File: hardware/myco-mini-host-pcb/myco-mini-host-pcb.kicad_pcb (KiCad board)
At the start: 2 copper layers, 190 x 115 mm, 22 parts, among them J1 Conn_01x17_Female, J2 Conn_01x17_Female, Q1 AO3401A, Q2 AO3401A, SW1 EM-04-Q, U1 XC9145B33C0R-G, U2 SHT40-AD1B-R2, U3 BH1750FVI-TR

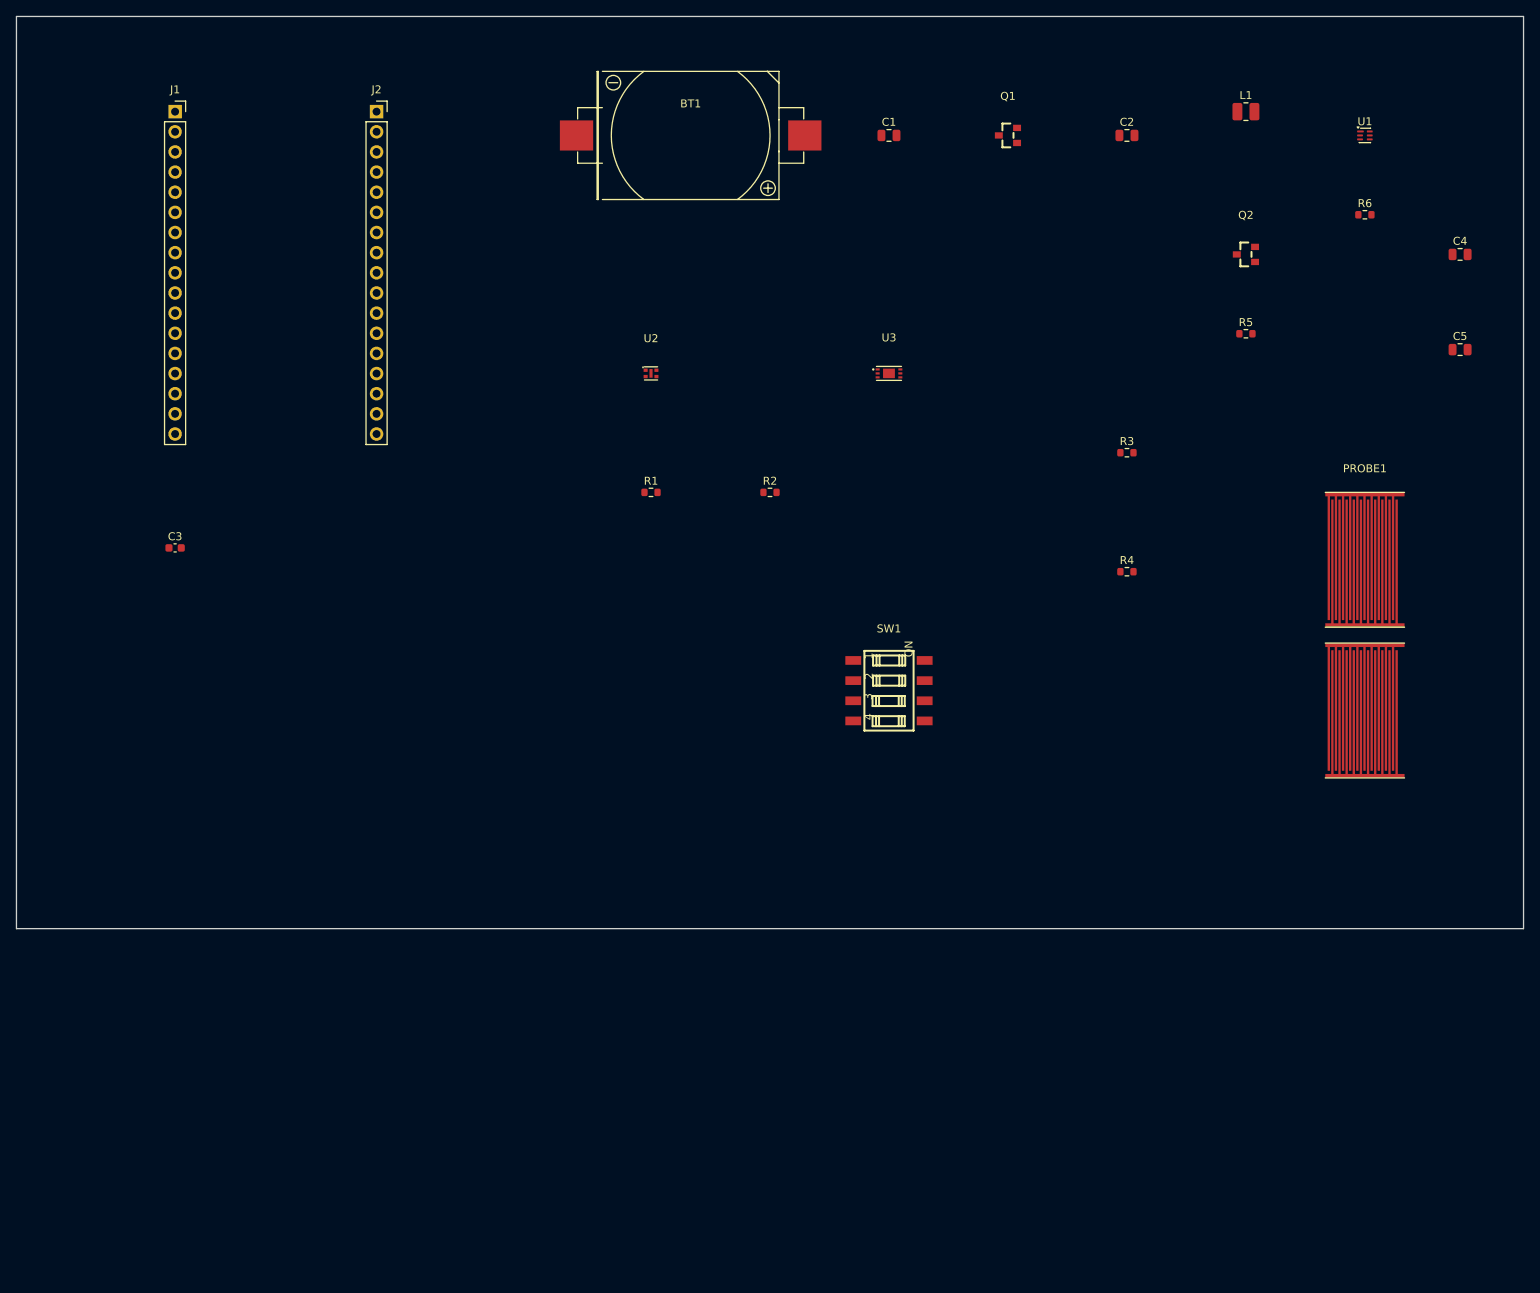
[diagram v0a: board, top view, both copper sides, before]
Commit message: fix: resolution XC9145 SOT-25, refonte sonde sol (profondeur), R3/R4 220k
- U1: XC9145B33C0R-G (WLP-6-05, non soudable a la main) -> XC9145B33CMR-G
  (SOT-25, LCSC C19261414, confirme en stock) - symbole/footprint refaits
- U2: SHT40 -> SHT41-AD1B-R2 (meme boitier/pinout, meilleure precision RH
  aux extremes)
- R3/R4: 1M -> 220k (1M hors plage source resistance max du SAADC nRF54L15,
  cf datasheet sec 11.17)
- Sonde sol: 36mm -> 60mm, doigts tournes a 90 (spines gauche/droite au
  lieu de haut/bas, moins fragiles mecaniquement), pitch 0.45mm -> 1.5mm
  et largeur 10mm -> 18mm pour la profondeur de penetration du champ dans
  le sol (~0.3mm -> ~1mm), compense par plus de doigts pour garder la
  capacite
- gen_pcb.py: PLACEMENT capture depuis le placement manuel valide (lecture
  seule du board actuel, pas de regeneration destructive)
- docs/pcb-design-decisions.md: sections 2.6/2.7/2.9/3.2 mises a jour avec
  le detail des calculs et sources
- misc/: ajout datasheet WLP-6-05 et reference Torex SOT-25 eval board

Co-Authored-By: Claude Sonnet 5 <noreply@anthropic.com>
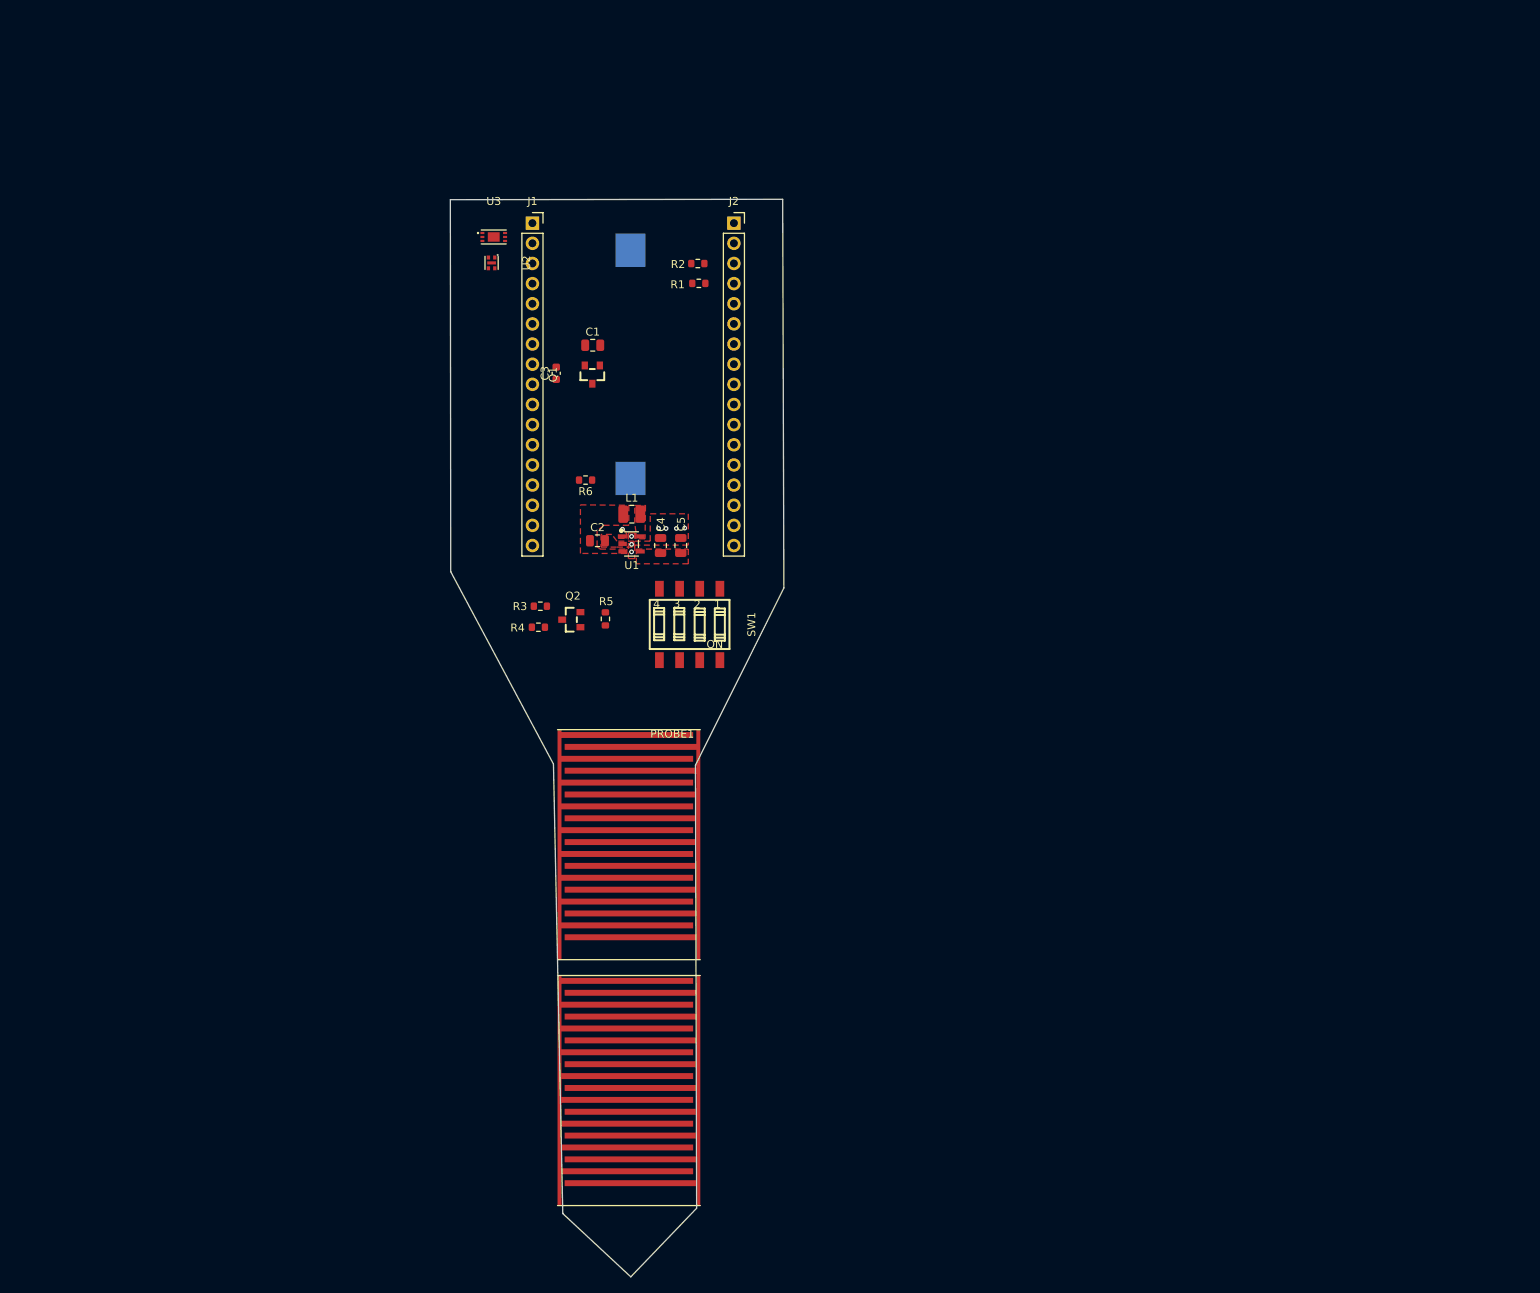
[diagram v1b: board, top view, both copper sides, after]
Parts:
- BT1: footprint BAT-TH_CR2032-BS-6-1 -> myco_host:BAT-TH_CR2032-BS-6-1; moved to B.Cu
- C1, C2, C4, C5: footprint C_0805_2012Metric -> Capacitor_SMD:C_0805_2012Metric
- C3: footprint C_0603_1608Metric -> Capacitor_SMD:C_0603_1608Metric
- J1, J2: footprint PinSocket_1x17_P2.54mm_Vertical -> Connector_PinSocket_2.54mm:PinSocket_1x17_P2.54mm_Vertical
- L1: footprint L_1008_2520Metric -> Inductor_SMD:L_1008_2520Metric
- PROBE1: footprint SOIL_PROBE_2SEG -> myco_host:SOIL_PROBE_2SEG
- Q1, Q2: footprint SOT-23_L2.9-W1.3-P1.90-LS2.4-BR -> myco_host:SOT-23_L2.9-W1.3-P1.90-LS2.4-BR
- R1, R2, R5, R6: footprint R_0603_1608Metric -> Resistor_SMD:R_0603_1608Metric
- R3, R4: value 1M -> 220k; footprint R_0603_1608Metric -> Resistor_SMD:R_0603_1608Metric
- SW1: footprint SW-SMD_8P-L10.1-W6.0-P2.54-LS9.8 -> myco_host:SW-SMD_8P-L10.1-W6.0-P2.54-LS9.8
- U1: value XC9145B33C0R-G -> XC9145B33CMR-G; footprint USON-6_XC9145_PLACEHOLDER -> myco_host:SOT-25-5_L2.9-W1.6-P0.95-LS2.8-BR
- U2: value SHT40-AD1B-R2 -> SHT41-AD1B-R2; footprint DFN-4_L1.5-W1.5-P0.8-TL-EP -> myco_host:DFN-4_L1.5-W1.5-P0.8-TL-EP
- U3: footprint WSOF-6_L2.6-W1.6-P0.50-TL-EP -> myco_host:WSOF-6_L2.6-W1.6-P0.50-TL-EP
- moved C4 107.3 mm to (81.2, 66.7), turned to 90 degrees
- moved U1 105.8 mm to (77.5, 66.5), turned to 180 degrees
- moved R6 103.8 mm to (71.8, 58.5), turned to 180 degrees
- moved C5 101.3 mm to (83.8, 66.7), turned to 90 degrees
- moved PROBE1 101.3 mm to (68.2, 89.9)
- moved Q2 96.7 mm to (70.0, 76.0)
- moved L1 92.6 mm to (77.6, 62.8)
- moved R5 88.4 mm to (74.2, 76.0), turned to -90 degrees
- moved C2 84.1 mm to (73.2, 66.1)
- moved R3 76.4 mm to (66.0, 74.3), turned to 180 degrees
- moved R4 74.5 mm to (65.8, 77.0), turned to 180 degrees
- moved Q1 60.5 mm to (72.6, 45.1), turned to 90 degrees
- moved C3 52.9 mm to (68.0, 45.0), turned to 90 degrees
- moved U3 52.7 mm to (60.2, 27.8)
- moved J2 47.2 mm to (90.5, 26.1)
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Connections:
- net BAT_RAW renamed /BAT_RAW
- net LX_NODE renamed Net-(U1-LX)
- net P0_02_SDA renamed /P0_02_SDA
- net P0_03_SCL renamed /P0_03_SCL
- net P1_04_SOIL_ADC2 renamed /P1_04_SOIL_ADC2
- net P1_07_SOIL_ADC1 renamed /P1_07_SOIL_ADC1
- net P1_14_SOIL_SW renamed /P1_14_SOIL_SW
- net P2_00_DIP0 renamed /P2_00_DIP0
- net P2_01_DIP1 renamed /P2_01_DIP1
- net P2_02_DIP2 renamed /P2_02_DIP2
- net P2_03_DIP3 renamed /P2_03_DIP3
- net SOIL_VCC renamed /SOIL_VCC
- C2 pad 1: VDD_NRF -> /VDD_NRF
- C3 pad 1: VDD_NRF -> /VDD_NRF
- C4 pad 1: VOUT_3V3 -> /VOUT_3V3
- C5 pad 1: VOUT_3V3 -> /VOUT_3V3
- J1 pad 10: (no net) -> unconnected-(J1-Pin_10-Pad10)
- J1 pad 11: (no net) -> unconnected-(J1-Pin_11-Pad11)
- J1 pad 13: (no net) -> unconnected-(J1-Pin_13-Pad13)
- J1 pad 14: (no net) -> unconnected-(J1-Pin_14-Pad14)
- J1 pad 16: (no net) -> unconnected-(J1-Pin_16-Pad16)
- J1 pad 17: (no net) -> unconnected-(J1-Pin_17-Pad17)
- J1 pad 2: (no net) -> unconnected-(J1-Pin_2-Pad2)
- J1 pad 3: (no net) -> unconnected-(J1-Pin_3-Pad3)
- J1 pad 4: (no net) -> unconnected-(J1-Pin_4-Pad4)
- J1 pad 5: (no net) -> unconnected-(J1-Pin_5-Pad5)
- J1 pad 6: P1_13_BOOST_EN -> /P1_13_BOOST_EN
- J1 pad 9: VDD_NRF -> /VDD_NRF
- J2 pad 1: (no net) -> unconnected-(J2-Pin_1-Pad1)
- J2 pad 10: (no net) -> unconnected-(J2-Pin_10-Pad10)
- J2 pad 11: (no net) -> unconnected-(J2-Pin_11-Pad11)
- J2 pad 12: (no net) -> unconnected-(J2-Pin_12-Pad12)
- J2 pad 13: (no net) -> unconnected-(J2-Pin_13-Pad13)
- J2 pad 2: (no net) -> unconnected-(J2-Pin_2-Pad2)
- J2 pad 5: (no net) -> unconnected-(J2-Pin_5-Pad5)
- J2 pad 6: (no net) -> unconnected-(J2-Pin_6-Pad6)
- J2 pad 7: (no net) -> unconnected-(J2-Pin_7-Pad7)
- J2 pad 8: (no net) -> unconnected-(J2-Pin_8-Pad8)
- J2 pad 9: (no net) -> unconnected-(J2-Pin_9-Pad9)
- L1 pad 1: VDD_NRF -> /VDD_NRF
- Q1 pad 3: VDD_NRF -> /VDD_NRF
- Q2 pad 2: VOUT_3V3 -> /VOUT_3V3
- R1 pad 1: VDD_NRF -> /VDD_NRF
- R2 pad 1: VDD_NRF -> /VDD_NRF
- R5 pad 1: VOUT_3V3 -> /VOUT_3V3
- R6 pad 1: P1_13_BOOST_EN -> /P1_13_BOOST_EN
- U1 pad 1: VDD_NRF -> /P1_13_BOOST_EN
- U1 pad 3: P1_13_BOOST_EN -> /VDD_NRF
- U1 pad 4: GND -> /VOUT_3V3
- U2 pad 3: VDD_NRF -> /VDD_NRF
- U3 pad 1: VOUT_3V3 -> /VOUT_3V3
- U3 pad 5: VDD_NRF -> /VDD_NRF
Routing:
- net GND: vias 0 -> 7
- net /P1_13_BOOST_EN: vias 0 -> 1
- added copper zone on F.Cu, net /P1_13_BOOST_EN
- added copper zone on F.Cu, net /VDD_NRF
- added copper zone on F.Cu, net /VOUT_3V3
- added copper zone on F.Cu, net GND
- added copper zone on F.Cu, net Net-(U1-LX)
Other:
- board size 190 x 115 mm -> 42 x 135.8 mm

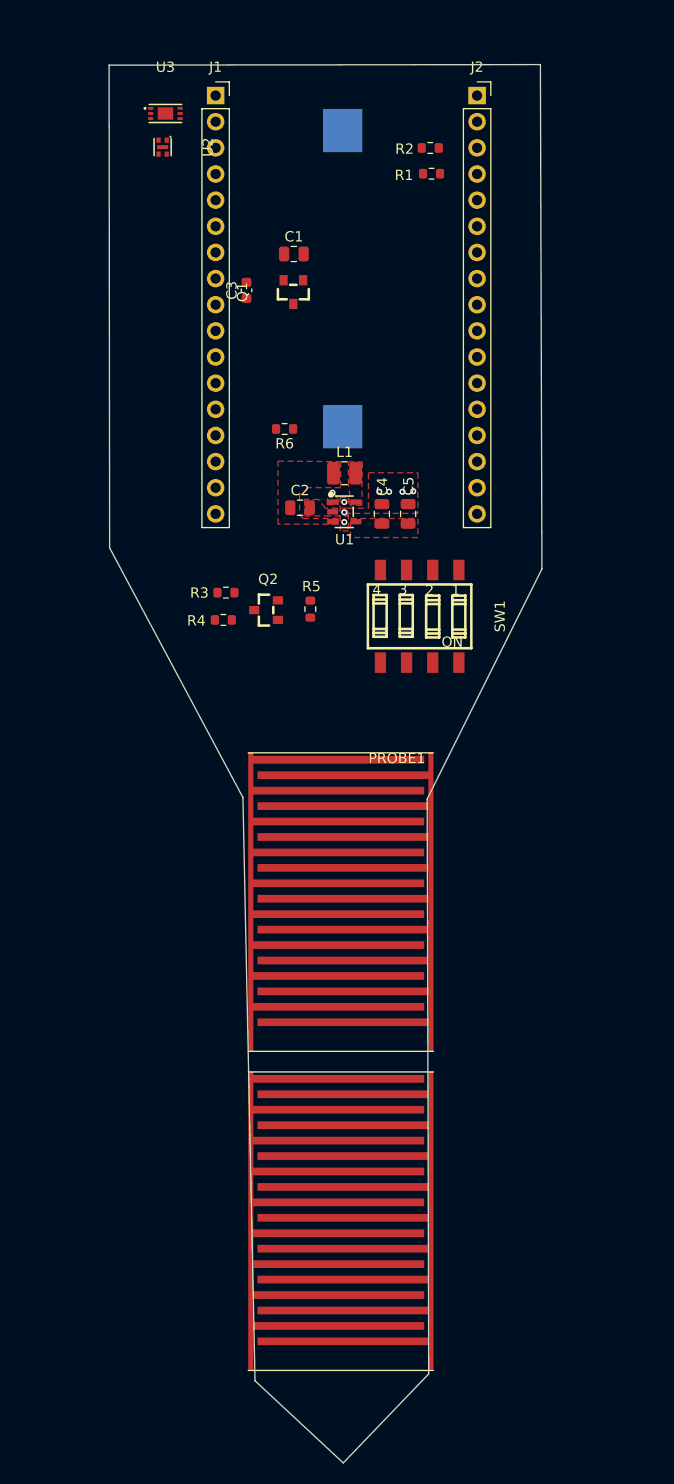
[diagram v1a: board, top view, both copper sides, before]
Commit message: feat: LED RGB feedback, decoupe thermique SHT41, contour symetrise, C6
Travail manuel de l'utilisateur dans l'éditeur KiCad (schéma + PCB),
documenté en détail dans docs/pcb-design-decisions.md (§2.10, §2.11) :

- LED RGB de feedback (D1, XL-5050RGBC) sur VOUT_3V3 — pinout corrigé
  après fourniture de la vraie datasheet Xinglight (3 LED indépendantes,
  pas anode commune ; l'hypothèse initiale inversait anode/cathode sur
  2 broches). Symbole/footprint refaits, câblage schéma corrigé
  chirurgicalement (add_rgb_led.py).
- Découpe thermique (3 fentes fermées) autour de U2 (SHT41), justifiée
  par le guide Sensirion (conduction thermique via PCB = source
  dominante d'erreur RH). Règle DRU mise à jour pour exclure U2 de la
  règle courtyard-to-edge.
- Contour de carte symétrisé par rapport à l'axe J1/J2 (X=77.75mm),
  recalculé par palier à partir des bounding boxes réelles des
  composants (premier essai par simple moyenne avait rogné dans U3/D1/
  R7-R9).
- C6 (100uF, decouplage) ajouté — cf. github issue #18.
- VDD SHT41/DVI BH1750 déjà déplacés vers VOUT_3V3 dans une session
  precedente (§2.5ter/§2.5quater), documentation mise à jour ici.

Aucune régénération gen_pcb.py/gen_schematic.py — édition manuelle
directe préservée (cf. mémoire feedback_pcb_placement).

Co-Authored-By: Claude Sonnet 5 <noreply@anthropic.com>
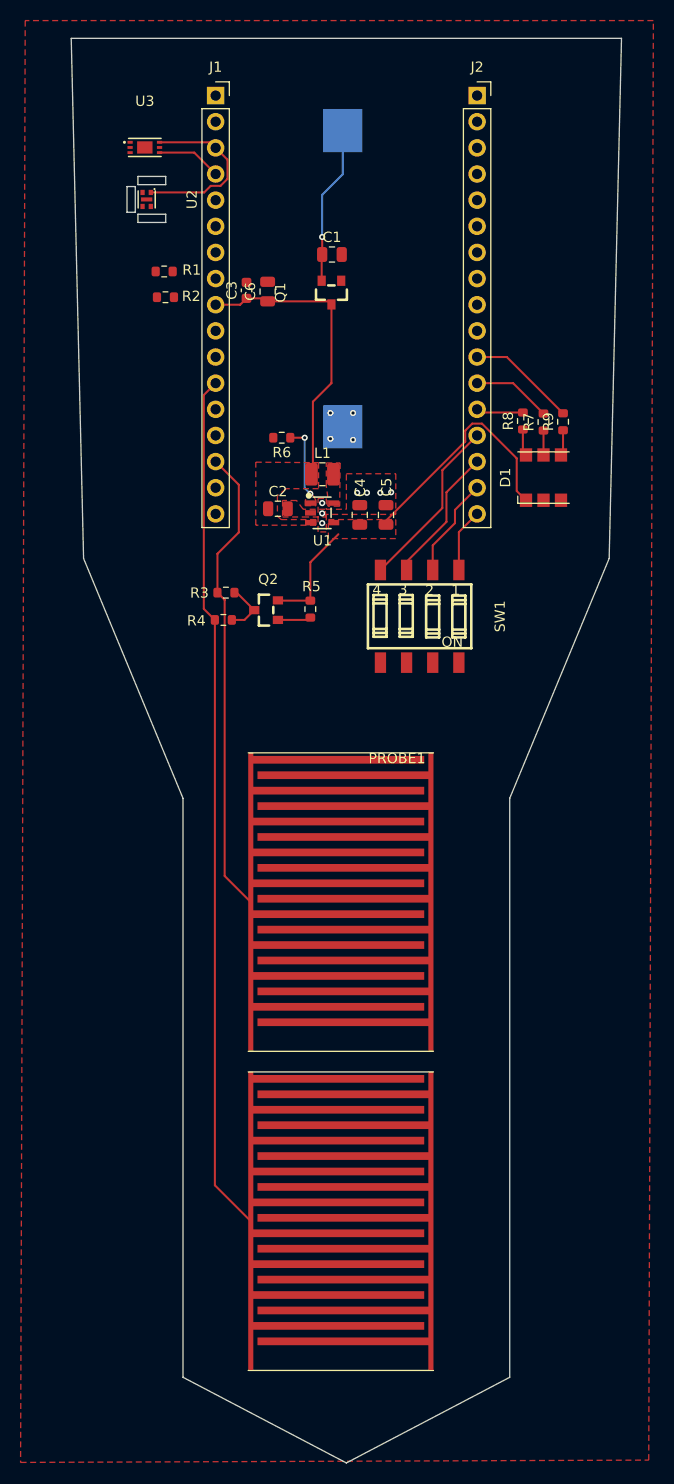
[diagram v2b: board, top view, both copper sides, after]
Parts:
- added C6: 100uF, Capacitor_SMD:C_0805_2012Metric, F.Cu at (70.1, 45.1)
- added D1: LED_RGB_5050_CA, myco_host:LED_SMD5050-6P, F.Cu at (96.9, 63.2)
- added R7: 220, Resistor_SMD:R_0603_1608Metric, F.Cu at (96.9, 57.8)
- added R8: 330, Resistor_SMD:R_0603_1608Metric, F.Cu at (94.9, 57.7)
- added R9: 330, Resistor_SMD:R_0603_1608Metric, F.Cu at (98.8, 57.8)
- moved R2 29.5 mm to (60.2, 45.6), turned to 180 degrees
- moved R1 27.7 mm to (60.0, 43.1), turned to 180 degrees
- moved U2 5.31 mm to (58.4, 36.1)
- moved U3 3.86 mm to (58.2, 31.1)
- moved Q1 3.70 mm to (76.3, 45.2)
- moved C1 3.70 mm to (76.3, 41.5)
- moved C2 2.15 mm to (71.1, 66.2)
- moved C4 2.15 mm to (79.0, 66.8)
- moved C5 2.15 mm to (81.6, 66.8)
- moved L1 2.15 mm to (75.4, 62.9)
- moved U1 2.15 mm to (75.4, 66.6)
- moved R6 0.89 mm to (71.5, 59.3)
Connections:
- J1 pad 3: unconnected-(J1-Pin_3-Pad3) -> /P1_10_SDA
- J1 pad 4: unconnected-(J1-Pin_4-Pad4) -> /P1_11_SCL
- J2 pad 11: unconnected-(J2-Pin_11-Pad11) -> /P2_06_LED_B
- J2 pad 12: unconnected-(J2-Pin_12-Pad12) -> /P2_05_LED_G
- J2 pad 13: unconnected-(J2-Pin_13-Pad13) -> /P2_04_LED_R
- R1 pad 1: /VDD_NRF -> /VOUT_3V3
- R1 pad 2: /P0_02_SDA -> /P1_10_SDA
- R2 pad 1: /VDD_NRF -> /VOUT_3V3
- R2 pad 2: /P0_03_SCL -> /P1_11_SCL
- U2 pad 1: /P0_02_SDA -> /P1_10_SDA
- U2 pad 2: /P0_03_SCL -> /P1_11_SCL
- U2 pad 3: /VDD_NRF -> /VOUT_3V3
- U3 pad 4: /P0_02_SDA -> /P1_11_SCL
- U3 pad 5: /VDD_NRF -> /VOUT_3V3
- U3 pad 6: /P0_03_SCL -> /P1_10_SDA
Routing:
- net /P1_04_SOIL_ADC2: track 0.00 -> 83.8 mm
- net /P1_07_SOIL_ADC1: track 0.00 -> 45.9 mm
- net /VOUT_3V3: track 0.00 -> 34.2 mm
- net /VDD_NRF: track 0.00 -> 30.4 mm
- net /P1_10_SDA: track 0.00 -> 17.2 mm
- net /P2_03_DIP3: track 0.00 -> 17.0 mm
- net /BAT_RAW: track 0.00 -> 15.4 mm, vias 0 -> 1
- net /P2_02_DIP2: track 0.00 -> 13.4 mm
- net /P2_06_LED_B: track 0.00 -> 10.6 mm
- net /P2_01_DIP1: track 0.00 -> 9.78 mm
- net /P2_05_LED_G: track 0.00 -> 7.67 mm
- net /P1_13_BOOST_EN: track 0.00 -> 7.08 mm, vias 1 -> 2
- net /P1_11_SCL: track 0.00 -> 6.40 mm
- net /P2_00_DIP0: track 0.00 -> 6.18 mm
- net /SOIL_VCC: track 0.00 -> 5.20 mm
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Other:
- board size 42 x 135.8 mm -> 53.5 x 138.4 mm
